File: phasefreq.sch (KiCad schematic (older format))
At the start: 93 parts, among them J1 Power Input, J2 RF Input, J3 LO Input, J4 VCO Tune, U1 LM317_3PinPackage, U2 LM337_SOT223, U3 ADCMP564, U4 AD9901, U5 LM4040DBZ-3, U6 AD8676, U7 AD8676

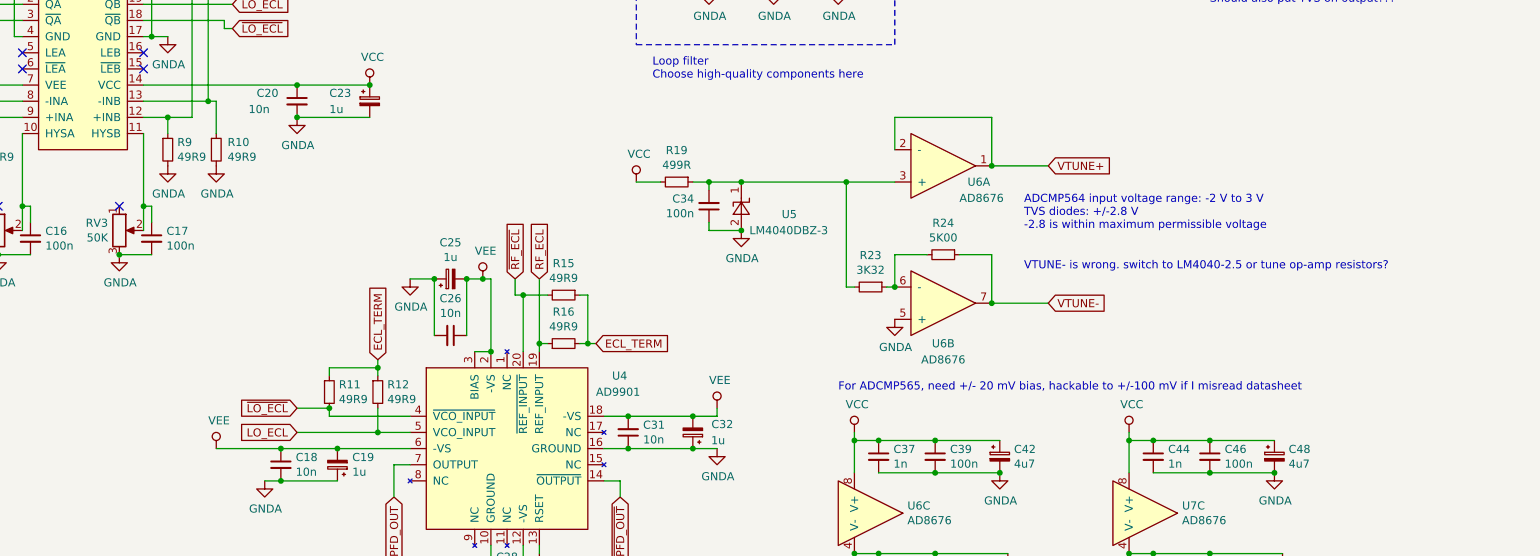
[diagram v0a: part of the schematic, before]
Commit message: Switched to Thevenin termination of inputs to AD9901
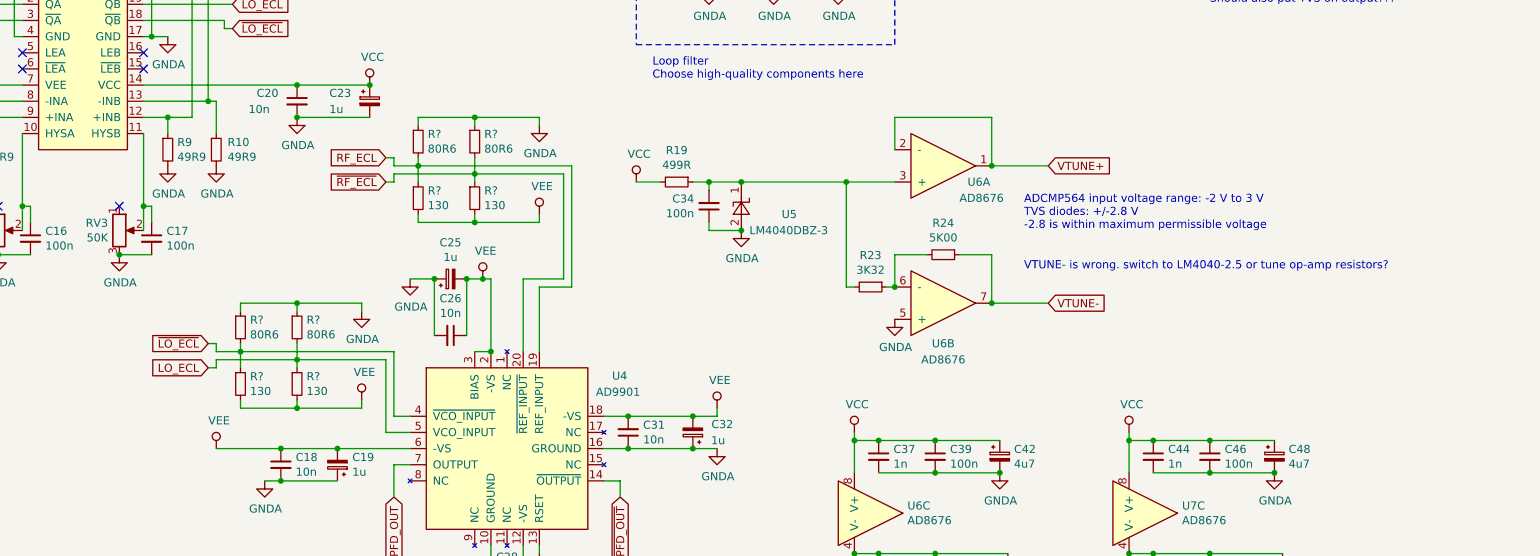
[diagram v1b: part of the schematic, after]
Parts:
- removed R11, R12, R15, R16: 49R9, Resistor_SMD:R_0603_1608Metric, symbol Device:R_Small
- added R? (x4): 80R6, symbol Device:R_Small
- added R? (x4): 130, symbol Device:R_Small
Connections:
- net GNDA: now also R?.1, R?.1, R?.1, R?.1
- net LO_ECL: now also R?.1, R?.2
- net RF_ECL: now also R?.1, R?.2
- net VEE: now also R?.2, R?.2, R?.2, R?.2
- net ~LO_ECL~: now also R?.1, R?.2
- net ~RF_ECL~: now also R?.1, R?.2
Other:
- note removed: "For ADCMP565, need +/- 20 mV bias, hackable to +/-100 mV if I misread datasheet"

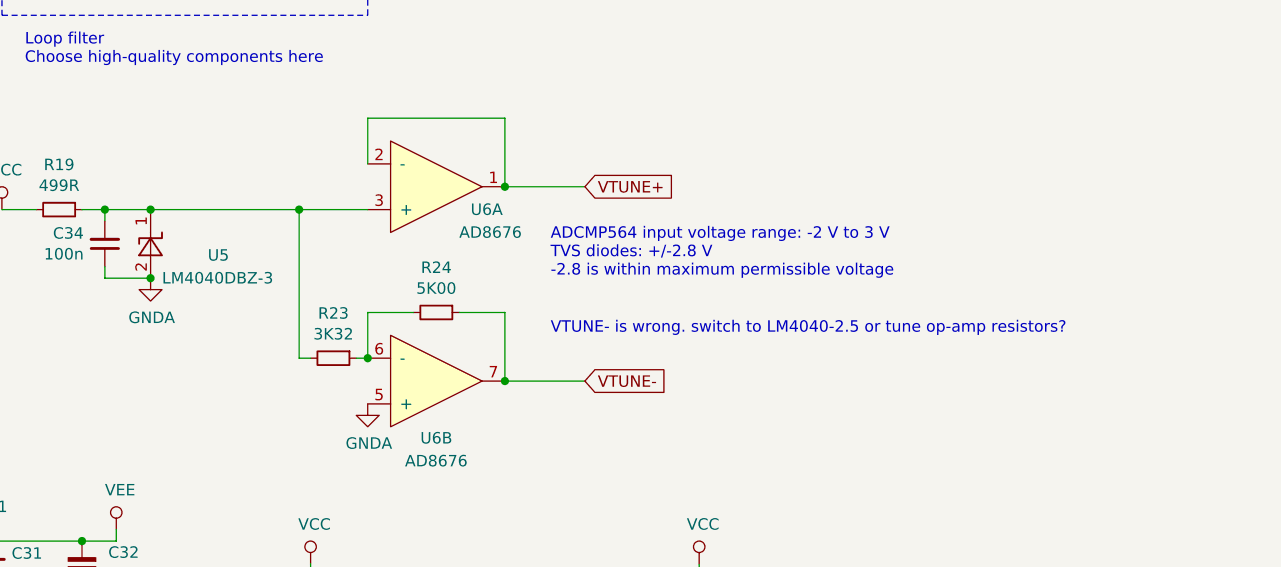
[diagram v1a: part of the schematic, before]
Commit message: changed Vbias to be +/- 2.5 V to accomodate TVS diodes
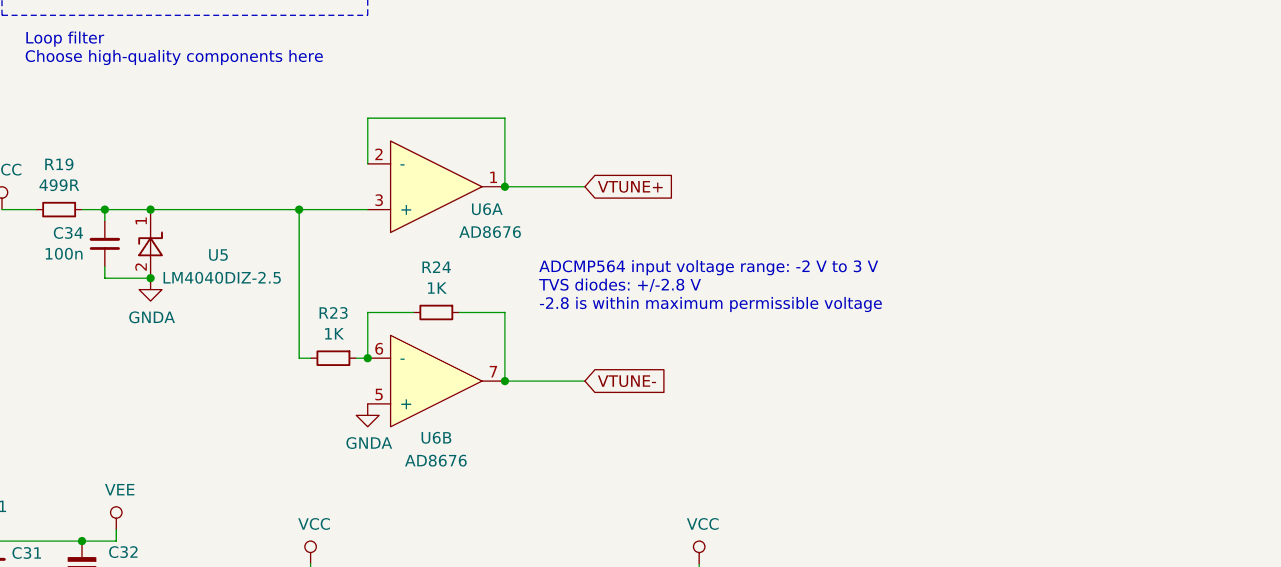
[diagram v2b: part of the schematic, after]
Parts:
- R23: value 3K32 -> 1K
- R24: value 5K00 -> 1K
- U5: value LM4040DBZ-3 -> LM4040DIZ-2.5
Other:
- note removed: "VTUNE- is wrong. switch to LM4040-2.5 or tune op-amp resistors?"
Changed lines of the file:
@@
 P 6850 3600
 F 0 "U5" V 6800 3850 50  0000 L CNN
-F 1 "LM4040DBZ-3" V 6700 3650 50  0000 L CNN
+F 1 "LM4040DIZ-2.5" V 6700 3650 50  0000 L CNN
 F 2 "Package_TO_SOT_SMD:SOT-23" H 6850 3400 50  0001 C CIN
 F 3 "http://www.ti.com/lit/ds/symlink/lm4040-n.pdf" H 6850 3600 50  0001 C CIN
@@
 P 7650 4100
 F 0 "R23" V 7454 4100 50  0000 C CNN
-F 1 "3K32" V 7545 4100 50  0000 C CNN
+F 1 "1K" V 7545 4100 50  0000 C CNN
 F 2 "Resistor_SMD:R_0603_1608Metric" H 7650 4100 50  0001 C CNN
 F 3 "~" H 7650 4100 50  0001 C CNN
@@
 P 8100 3900
 F 0 "R24" V 7904 3900 50  0000 C CNN
-F 1 "5K00" V 7995 3900 50  0000 C CNN
+F 1 "1K" V 7995 3900 50  0000 C CNN
 F 2 "Resistor_SMD:R_0603_1608Metric" H 8100 3900 50  0001 C CNN
 F 3 "~" H 8100 3900 50  0001 C CNN
@@
 Wire Wire Line
 	6200 3450 6350 3450
-Text Notes 8600 3750 0    50   ~ 0
+Text Notes 8550 3900 0    50   ~ 0
 ADCMP564 input voltage range: -2 V to 3 V\nTVS diodes: +/-2.8 V\n-2.8 is within maximum permissible voltage
-Text Notes 8600 4000 0    50   ~ 0
-VTUNE- is wrong. switch to LM4040-2.5 or tune op-amp resistors?
 $Comp
 L grav:SLVU2.8-8 D?

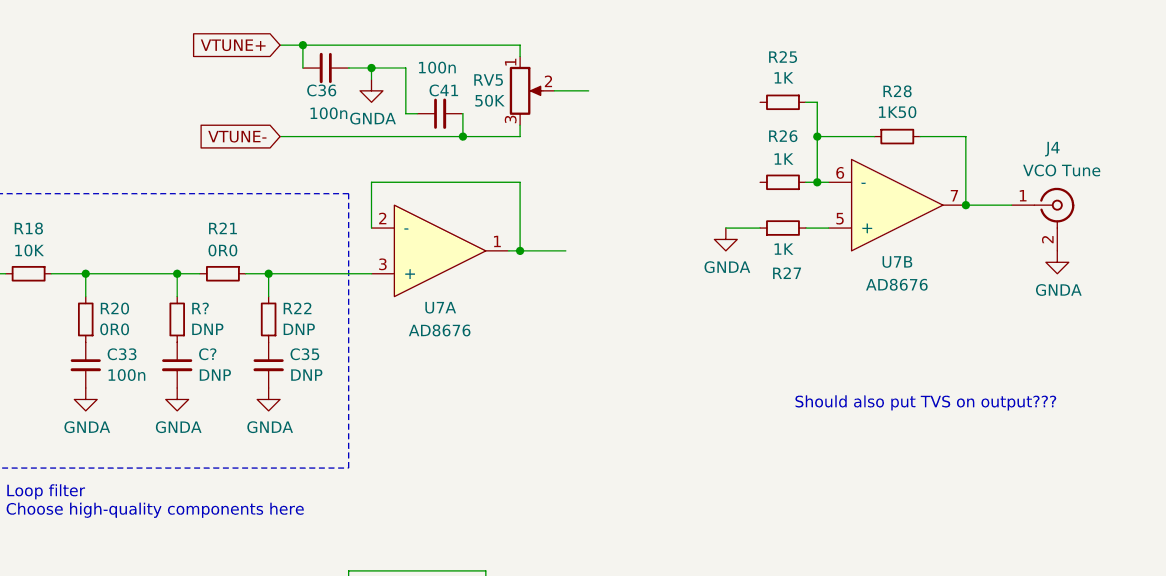
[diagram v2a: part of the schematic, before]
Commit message: Set offset on output to match possible PLL filter outputs, checked LM4040-2.5 resistor value
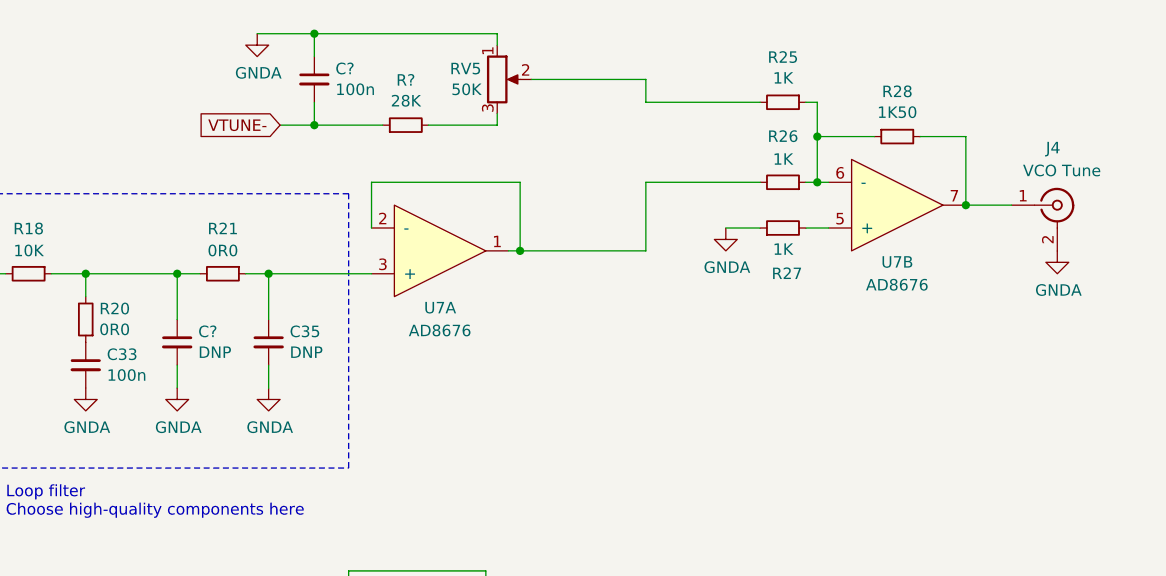
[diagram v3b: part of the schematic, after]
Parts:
- removed C36, C41: 100n, Capacitor_SMD:C_0603_1608Metric, symbol Device:C_Small
- removed R22, R?: DNP, Resistor_SMD:R_0603_1608Metric, symbol Device:R_Small
- added C?: 100n, symbol Device:C_Small
- added R?: 28K, symbol Device:R_Small
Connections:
- net GNDA: now also RV5.1, C?.1
- net VTUNE+: no longer RV5.1
- net VTUNE-: now also C?.2, R?.1; no longer RV5.3
- net at R18.1, R20.2, R21.2: now also C?.1
- net at R26.2: now also U7.1, U7.2 (-)
- net at R25.2: now also RV5.2
- net at R21.1, U7.3 (+): now also C35.1
- new net: R?.2, RV5.3
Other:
- note removed: "Should also put TVS on output???"
- moved on the sheet: C35, C?, RV5
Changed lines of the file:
@@
 	10500 1150 10500 1450
-$Comp
-L Device:C_Small C36
-U 1 1 5DF0D92D
-P 7700 850
-F 0 "C36" V 7600 900 50  0000 R CNN
-F 1 "100n" V 7500 950 50  0000 R CNN
-F 2 "Capacitor_SMD:C_0603_1608Metric" H 7700 850 50  0001 C CNN
-F 3 "~" H 7700 850 50  0001 C CNN
-	1    7700 850
-	0    1    -1   0
-$EndComp
 $Comp
 L Device:R_POT RV5
 U 1 1 5DF10BE3
-P 8550 950
-F 0 "RV5" H 8481 996 50  0000 R CNN
-F 1 "50K" H 8481 905 50  0000 R CNN
-F 2 "Potentiometer_SMD:Potentiometer_Vishay_TS53YJ_Vertical" H 8550 950 50  0001 C CNN
-F 3 "~" H 8550 950 50  0001 C CNN
-	1    8550 950
-	1    0    0    -1
-$EndComp
-Wire Wire Line
-	8550 1150 8550 1100
-Wire Wire Line
-	8550 800  8550 750
+P 8450 900
+F 0 "RV5" H 8381 946 50  0000 R CNN
+F 1 "50K" H 8381 855 50  0000 R CNN
+F 2 "Potentiometer_SMD:Potentiometer_Vishay_TS53YJ_Vertical" H 8450 900 50  0001 C CNN
+F 3 "~" H 8450 900 50  0001 C CNN
+	1    8450 900
+	1    0    0    -1
+$EndComp
+Wire Wire Line
+	8450 1100 8450 1050
+Wire Wire Line
+	8450 750  8450 700
 $Comp
 L Connector:Conn_Coaxial J4
@@
 	1    0    0    1
 $EndComp
-Text GLabel 7500 750  0    50   Input ~ 0
-VTUNE+
-Wire Wire Line
-	8550 1650 8750 1650
 $Comp
 L power:GNDA #PWR029
@@
 L Device:C_Small C35
 U 1 1 5E2D217A
-P 7450 2150
-F 0 "C35" H 7542 2196 50  0000 L CNN
-F 1 "DNP" H 7542 2105 50  0000 L CNN
-F 2 "Capacitor_SMD:C_0603_1608Metric" H 7450 2150 50  0001 C CNN
-F 3 "~" H 7450 2150 50  0001 C CNN
-	1    7450 2150
+P 7450 2050
+F 0 "C35" H 7542 2096 50  0000 L CNN
+F 1 "DNP" H 7542 2005 50  0000 L CNN
+F 2 "Capacitor_SMD:C_0603_1608Metric" H 7450 2050 50  0001 C CNN
+F 3 "~" H 7450 2050 50  0001 C CNN
+	1    7450 2050
 	1    0    0    -1
 $EndComp
@@
 $EndComp
 $Comp
-L Device:C_Small C41
-U 1 1 5E39A406
-P 8200 1050
-F 0 "C41" V 8100 1100 50  0000 R CNN
-F 1 "100n" V 8000 1150 50  0000 R CNN
-F 2 "Capacitor_SMD:C_0603_1608Metric" H 8200 1050 50  0001 C CNN
-F 3 "~" H 8200 1050 50  0001 C CNN
-	1    8200 1050
-	0    -1   1    0
-$EndComp
-$Comp
 L power:GNDA #PWR026
 U 1 1 5E3FF178
-P 7900 900
-F 0 "#PWR026" H 7900 650 50  0001 C CNN
-F 1 "GNDA" H 7905 727 50  0000 C CNN
-F 2 "" H 7900 900 50  0001 C CNN
-F 3 "" H 7900 900 50  0001 C CNN
-	1    7900 900
-	1    0    0    -1
-$EndComp
-Wire Wire Line
-	7800 850  7900 850
-Wire Wire Line
-	7900 850  7900 900
-Wire Wire Line
-	8050 1050 8050 850
-Wire Wire Line
-	8050 850  7900 850
-Connection ~ 7900 850
-Wire Wire Line
-	8300 1050 8300 1150
-Connection ~ 8300 1150
-Wire Wire Line
-	8300 1150 8550 1150
-Wire Wire Line
-	7600 850  7600 750
-Wire Wire Line
-	8100 1050 8050 1050
-Wire Wire Line
-	7500 750  7600 750
-Connection ~ 7600 750
-Wire Wire Line
-	7600 750  8550 750
-Wire Wire Line
-	7500 1150 8300 1150
-Wire Wire Line
-	8700 950  8850 950
+P 7400 700
+F 0 "#PWR026" H 7400 450 50  0001 C CNN
+F 1 "GNDA" H 7405 527 50  0000 C CNN
+F 2 "" H 7400 700 50  0001 C CNN
+F 3 "" H 7400 700 50  0001 C CNN
+	1    7400 700
+	1    0    0    -1
+$EndComp
 Text GLabel 8750 4200 2    50   Input ~ 0
 VTUNE-
@@
 Wire Wire Line
 	3100 1250 3100 1350
-Text Notes 9750 2350 0    50   ~ 0
-Should also put TVS on output???
 Connection ~ 4550 2850
 Wire Wire Line
@@
 L Device:C_Small C?
 U 1 1 5DFC0EDB
-P 7050 2150
-F 0 "C?" H 7142 2196 50  0000 L CNN
-F 1 "DNP" H 7142 2105 50  0000 L CNN
-F 2 "Capacitor_SMD:C_0603_1608Metric" H 7050 2150 50  0001 C CNN
-F 3 "~" H 7050 2150 50  0001 C CNN
-	1    7050 2150
+P 7050 2050
+F 0 "C?" H 7142 2096 50  0000 L CNN
+F 1 "DNP" H 7142 2005 50  0000 L CNN
+F 2 "Capacitor_SMD:C_0603_1608Metric" H 7050 2050 50  0001 C CNN
+F 3 "~" H 7050 2050 50  0001 C CNN
+	1    7050 2050
 	1    0    0    -1
 $EndComp
@@
 	1    0    0    -1
 $EndComp
-Text GLabel 7500 1150 0    50   Input ~ 0
+Text GLabel 7500 1100 0    50   Input ~ 0
 VTUNE-
-$Comp
-L Device:R_Small R22
-U 1 1 5E2D2174
-P 7450 1950
-F 0 "R22" H 7391 1904 50  0000 R CNN
-F 1 "DNP" H 7391 1995 50  0000 R CNN
-F 2 "Resistor_SMD:R_0603_1608Metric" H 7450 1950 50  0001 C CNN
-F 3 "~" H 7450 1950 50  0001 C CNN
-	1    7450 1950
-	-1   0    0    1
-$EndComp
-$Comp
-L Device:R_Small R?
-U 1 1 5E07336D
-P 7050 1950
-F 0 "R?" H 6991 1904 50  0000 R CNN
-F 1 "DNP" H 6991 1995 50  0000 R CNN
-F 2 "Resistor_SMD:R_0603_1608Metric" H 7050 1950 50  0001 C CNN
-F 3 "~" H 7050 1950 50  0001 C CNN
-	1    7050 1950
-	-1   0    0    1
-$EndComp
 Wire Wire Line
 	6500 1750 6650 1750
-Wire Wire Line
-	7050 1850 7050 1750
 Connection ~ 7050 1750
 Wire Wire Line
@@
 Wire Wire Line
 	7350 1750 7450 1750
-Wire Wire Line
-	7450 1750 7450 1850
 Wire Notes Line
 	6200 1400 6200 2600
@@
 Wire Wire Line
 	5600 4100 5600 4500
+$Comp
+L Device:C_Small C?
+U 1 1 5E1F7DC1
+P 7650 900
+F 0 "C?" H 7742 946 50  0000 L CNN
+F 1 "100n" H 7742 855 50  0000 L CNN
+F 2 "" H 7650 900 50  0001 C CNN
+F 3 "~" H 7650 900 50  0001 C CNN
+	1    7650 900
+	1    0    0    -1
+$EndComp
+Wire Wire Line
+	7650 1000 7650 1100
+Wire Wire Line
+	7650 1100 7500 1100
+Wire Wire Line
+	7650 800  7650 700
+Connection ~ 7650 700
+Wire Wire Line
+	7400 700  7650 700
+$Comp
+L Device:R_Small R?
+U 1 1 5E286A64
+P 8050 1100
+F 0 "R?" V 8246 1100 50  0000 C CNN
+F 1 "28K" V 8155 1100 50  0000 C CNN
+F 2 "" H 8050 1100 50  0001 C CNN
+F 3 "~" H 8050 1100 50  0001 C CNN
+	1    8050 1100
+	0    -1   -1   0
+$EndComp
+Wire Wire Line
+	7650 1100 7950 1100
+Connection ~ 7650 1100
+Wire Wire Line
+	8150 1100 8450 1100
+Wire Wire Line
+	7650 700  8450 700
+Wire Wire Line
+	9100 900  9100 1000
+Wire Wire Line
+	9100 1000 9600 1000
+Wire Wire Line
+	8600 900  9100 900
+Wire Wire Line
+	9100 1650 9100 1350
+Wire Wire Line
+	9100 1350 9600 1350
+Wire Wire Line
+	8550 1650 9100 1650
+Wire Wire Line
+	7450 1750 7450 1950
+Wire Wire Line
+	7050 1750 7050 1950
+Wire Wire Line
+	7050 2150 7050 2250
+Wire Wire Line
+	7450 2150 7450 2250
 $EndSCHEMATC
